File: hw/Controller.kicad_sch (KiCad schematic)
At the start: 44 parts, among them J201 Conn_01x08, J202 Molex-105017-0001, J203 Conn_01x03, J204 Conn_01x02, J205 Conn_01x02, J206 Conn_01x02, J207 Conn_01x02, P201 Current-Probe, Q201 DTC114EE, U201 STM32F401XX-LQFP64, U202 TLV62150A, X201 Mounting-Hole-M3, X202 Mounting-Hole-M3, X203 Mounting-Hole-M3, X204 Mounting-Hole-M3, Y201 MCSJK-7I-8.00-18-30-60-B-30

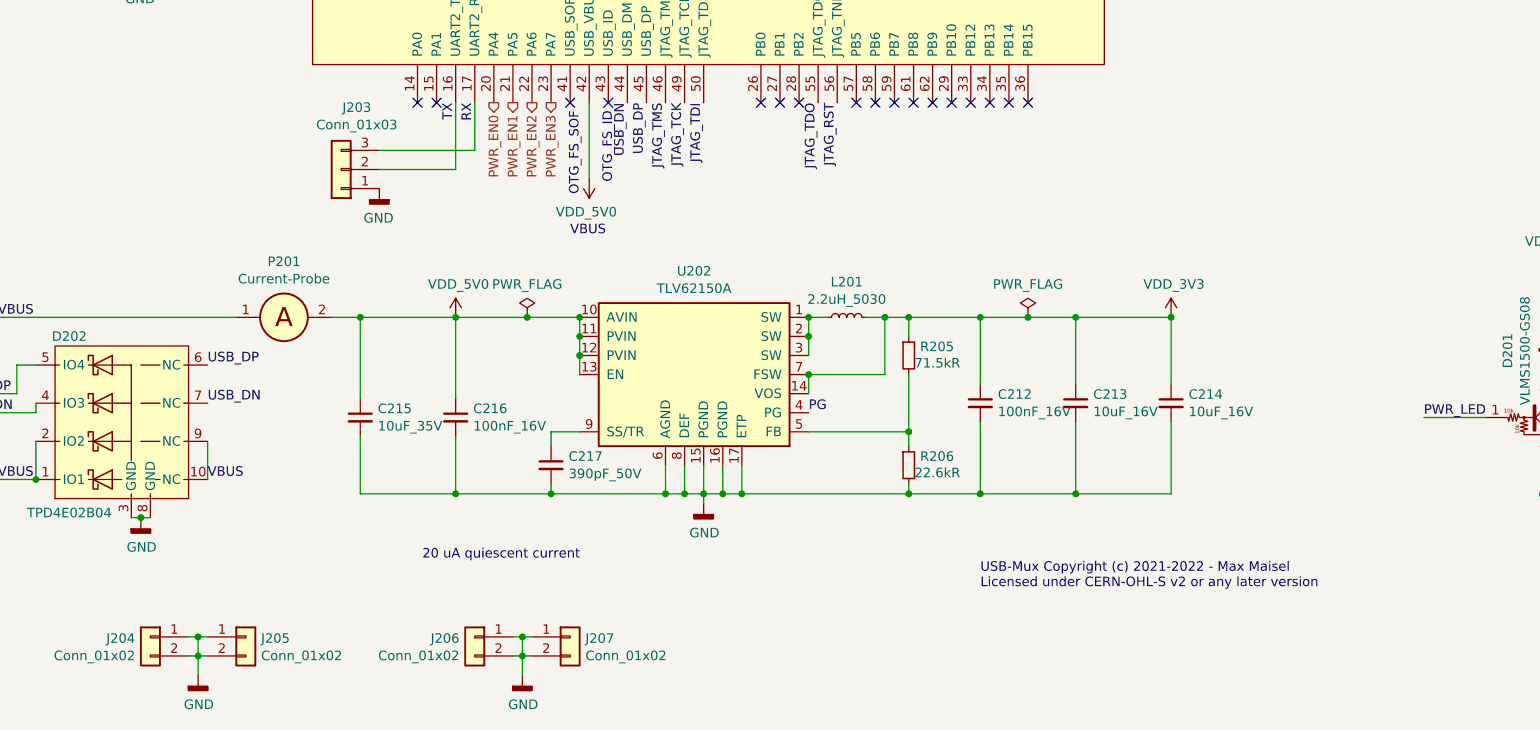
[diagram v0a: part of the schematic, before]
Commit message: Mark dnp components in schematic.
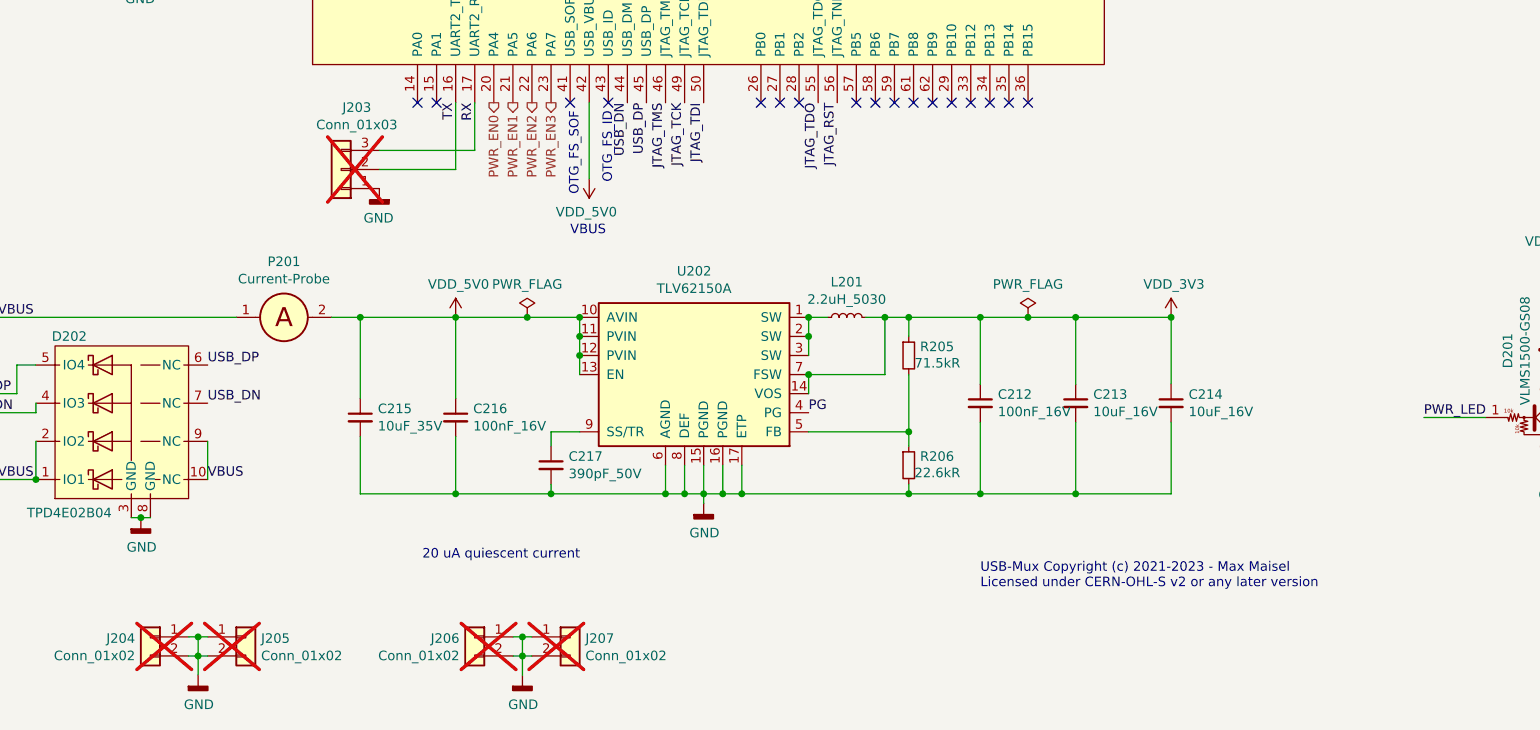
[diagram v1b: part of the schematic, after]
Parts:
- J203, J204, J205, J206, J207: now not fitted
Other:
- note added: "USB-Mux Copyright (c) 2021-2023 - Max Maisel Licensed under CERN-OHL-S v2 or any later version"
- note removed: "USB-Mux Copyright (c) 2021-2022 - Max Maisel Licensed under CERN-OHL-S v2 or any later version"
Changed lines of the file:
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@@
     (stroke (width 0) (type default))
   )
-  (text "USB-Mux Copyright (c) 2021-2022 - Max Maisel\nLicensed under CERN-OHL-S v2 or any later version"
+  (text "USB-Mux Copyright (c) 2021-2023 - Max Maisel\nLicensed under CERN-OHL-S v2 or any later version"
     (at 177.8 171.45 0)
     (effects (font (size 1.27 1.27)) (justify left bottom))
@@
   )
   (symbol (lib_id "USB-Mux:Conn_01x02") (at 80.01 179.07 0) (unit 1)
-    (in_bom yes) (on_board yes) (dnp no)
+    (in_bom yes) (on_board yes) (dnp yes)
     (property "Reference" "J205" (at 82.042 178.0032 0)
       (effects (font (size 1.27 1.27)) (justify left))
@@
   )
   (symbol (lib_id "USB-Mux:Conn_01x02") (at 123.19 179.07 0) (unit 1)
-    (in_bom yes) (on_board yes) (dnp no)
+    (in_bom yes) (on_board yes) (dnp yes)
     (property "Reference" "J207" (at 125.222 178.0032 0)
       (effects (font (size 1.27 1.27)) (justify left))
@@
   )
   (symbol (lib_id "USB-Mux:Conn_01x02") (at 67.31 179.07 0) (mirror y) (unit 1)
-    (in_bom yes) (on_board yes) (dnp no)
+    (in_bom yes) (on_board yes) (dnp yes)
     (property "Reference" "J204" (at 65.278 178.0032 0)
       (effects (font (size 1.27 1.27)) (justify left))
@@
   )
   (symbol (lib_id "USB-Mux:Conn_01x02") (at 110.49 179.07 0) (mirror y) (unit 1)
-    (in_bom yes) (on_board yes) (dnp no)
+    (in_bom yes) (on_board yes) (dnp yes)
     (property "Reference" "J206" (at 108.458 178.0032 0)
       (effects (font (size 1.27 1.27)) (justify left))
@@
   )
   (symbol (lib_id "USB-Mux:Conn_01x03") (at 92.71 115.57 180) (unit 1)
-    (in_bom yes) (on_board yes) (dnp no)
+    (in_bom yes) (on_board yes) (dnp yes)
     (property "Reference" "J203" (at 94.7928 107.315 0)
       (effects (font (size 1.27 1.27)))

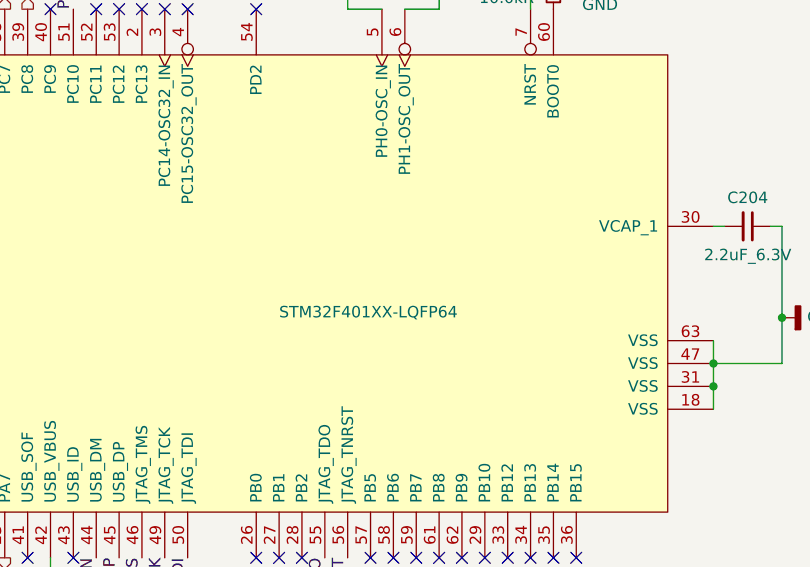
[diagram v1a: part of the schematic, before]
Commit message: Add some missing component ordering numbers.
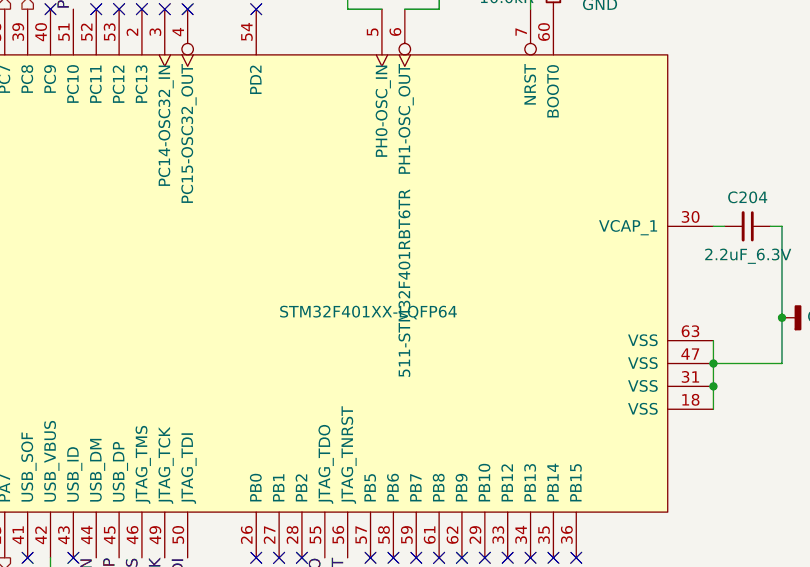
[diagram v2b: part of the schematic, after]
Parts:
- U201: mouser# (none) -> 511-STM32F401RBT6TR
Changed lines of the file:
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@@
       (effects (font (size 1.27 1.27)) hide)
+    )
+    (property "mouser#" "511-STM32F401RBT6TR" (at 165.1 76.2 0)
+      (effects (font (size 1.27 1.27)))
     )
     (pin "1")
